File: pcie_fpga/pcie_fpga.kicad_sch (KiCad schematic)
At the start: 18 parts, among them J3 Bus_PCI_Express_x4, U1 XC7A50T-FGG484, U2 LTC6957xMS-2, X1 ECS-2520MVQ-1000-BN-TR

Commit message: brought in the lucanastasio PCIe board template
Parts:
- removed C1, C11, C2, C3, C4, C5, C6, C7, C8, C9: 0.01uf, Capacitor_SMD:C_0603_1608Metric, symbol Device:C
- removed D3: LED, LED_SMD:LED_0603_1608Metric, symbol Device:LED
- removed J3: Bus_PCI_Express_x4, Connector_PCBEdge:BUS_PCIexpress_x4, symbol Connector:Bus_PCI_Express_x4
- removed R2: 49.9, Resistor_SMD:R_0603_1608Metric, symbol Device:R
- removed R3: 240, Resistor_SMD:R_0603_1608Metric, symbol Device:R
- removed U2: LTC6957xMS-2, Package_SO:MSOP-12_3x4mm_P0.65mm, symbol Interface:LTC6957xMS-2
- added J2: PCIexpress_x4, PCIexpress:PCIexpress_x4, symbol PCIexpress:PCIexpress_x4
- R1: value 100 -> 10
- U1: footprint Package_BGA:BGA-484_23.0x23.0mm_Layout22x22_P1.0mm -> Package_BGA:Xilinx_FGG484
- U1: footprint Package_BGA:BGA-484_23.0x23.0mm_Layout22x22_P1.0mm -> (none)
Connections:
- net +3V3: now also J2.A10 (+3.3V), J2.A9 (+3.3V), J2.B8 (+3.3V)
- net GND: now also J2.A12 (GND), J2.A15 (GND), J2.A18 (GND), J2.A20 (GND), J2.A23 (GND), J2.A24 (GND), J2.A27 (GND), J2.A28 (GND), J2.A31 (GND), J2.A4 (GND), J2.B13 (GND), J2.B16 (GND), J2.B18 (GND), J2.B21 (GND), J2.B22 (GND), J2.B25 (GND), J2.B26 (GND), J2.B29 (GND), J2.B32 (GND), J2.B4 (GND), J2.B7 (GND)
- net fpga_clk: now reaches R1.1
- new net +12V: J2.A2 (+12V), J2.A3 (+12V), J2.B1 (+12V), J2.B2 (+12V), J2.B3 (+12V)
- new net +3.3VA: J2.B10 (+3.3V_aux)
- new net prsntn: J2.A1 (~{PRSNT1}), J2.B31 (~{PRSNT2})
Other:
- note added: "From add-in card transmitter to mainboard receiver Place AC coupling capacitors here if necessary"
- note added: "From mainboard transmitter to add-in card receiver Place termination resistors here if necessary"
- note removed: "This is a M-key M.2 connector for an NVMe SSD."
- note removed: "www.hdlguy.com"

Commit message: adding more fpga stuff
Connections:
- net +3V3: now also U1.AA17 (VCCO_13), U1.AB14 (VCCO_13), U1.M14 (VCCO_14), U1.P18 (VCCO_14), U1.R15 (VCCO_14), U1.T22 (VCCO_14), U1.U19 (VCCO_14), U1.V16 (VCCO_13), U1.W13 (VCCO_13), U1.Y10 (VCCO_13), U1.Y20 (VCCO_14)
- net GND: now also U1.A11 (GND), U1.A12 (GND), U1.A2 (GND), U1.A22 (GND), U1.A3 (GND), U1.A5 (GND), U1.A7 (GND), U1.A9 (GND), U1.AA12 (GND), U1.AA2 (GND), U1.AA22 (GND), U1.AB19 (GND), U1.AB9 (GND), U1.B12 (GND), U1.B19 (GND), U1.B3 (GND), U1.C10 (GND), U1.C12 (GND), U1.C16 (GND), U1.C3 (GND), U1.C6 (GND), U1.D12 (GND), U1.D13 (GND), U1.D3 (GND), U1.D4 (GND), U1.D8 (GND), U1.E11 (GND), U1.E12 (VCCBATT_0), U1.E20 (GND), U1.E4 (GND), U1.E5 (GND), U1.E7 (GND), U1.E9 (GND), U1.F11 (GND), U1.F17 (GND), U1.F5 (GND), U1.G10 (GND), U1.G12 (GND), U1.G14 (GND), U1.G5 (GND), U1.G6 (GND), U1.G7 (GND), U1.G8 (GND), U1.G9 (GND), U1.H1 (GND), U1.H11 (GND), U1.H21 (GND), U1.H7 (GND), U1.H9 (GND), U1.J10 (GND), U1.J12 (GND), U1.J18 (GND), U1.J8 (GND), U1.K11 (GND), U1.K15 (GND), U1.K5 (GND), U1.K7 (GND), U1.K9 (GNDADC_0), U1.L2 (GND), U1.L22 (GND), U1.L8 (GND), U1.M11 (GND), U1.M19 (GND), U1.M7 (GND), U1.N16 (GND), U1.N6 (GND), U1.N8 (GND), U1.P11 (GND), U1.P13 (GND), U1.P3 (GND), U1.P7 (GND), U1.P9 (GND), U1.R10 (GND), U1.R12 (GND), U1.R20 (GND), U1.R8 (GND), U1.T11 (GND), U1.T17 (GND), U1.T7 (GND), U1.T9 (GND), U1.U14 (GND), U1.U4 (GND), U1.V1 (GND), U1.V11 (GND), U1.V21 (GND), U1.W18 (GND), U1.W8 (GND), U1.Y15 (GND), U1.Y5 (GND)
- net fpga_clk: now also U1.W19 (IO_L12P_T1_MRCC_14)
- net perstn: now reaches U1.N15 (IO_25_14)
- net perstn: now also J2.A11 (~{PERST})
- net refclk_P: now reaches J2.A13 (REFCLK+)
- net refclk_P: now also U1.F6 (MGTREFCLK0P_216)
- net refclk_N: now reaches J2.A14 (REFCLK-)
- net refclk_N: now also U1.E6 (MGTREFCLK0N_216)
- net per0_P: now reaches J2.A16 (PERp0)
- net per0_P: now also U1.B4 (MGTPTXP0_216)
- net per0_N: now reaches J2.A17 (PERn0)
- net per0_N: now also U1.A4 (MGTPTXN0_216)
- net per1_P: now reaches J2.A21 (PERp1)
- net per1_P: now also U1.D5 (MGTPTXP1_216)
- net per1_N: now reaches J2.A22 (PERn1)
- net per1_N: now also U1.C5 (MGTPTXN1_216)
- net per2_P: now reaches J2.A25 (PERp2)
- net per2_P: now also U1.B6 (MGTPTXP2_216)
- net per2_N: now reaches J2.A26 (PERn2)
- net per2_N: now also U1.A6 (MGTPTXN2_216)
- net per3_P: now reaches J2.A29 (PERp3)
- net per3_P: now also U1.D7 (MGTPTXP3_216)
- net per3_N: now reaches J2.A30 (PERn3)
- net per3_N: now also U1.C7 (MGTPTXN3_216)
- net pet0_P: now reaches J2.B14 (PETp0)
- net pet0_P: now also U1.B8 (MGTPRXP0_216)
- net pet0_N: now reaches J2.B15 (PETn0)
- net pet0_N: now also U1.A8 (MGTPRXN0_216)
- net pet1_P: now reaches J2.B19 (PETp1)
- net pet1_P: now also U1.D11 (MGTPRXP1_216)
- net pet1_N: now reaches J2.B20 (PETn1)
- net pet1_N: now also U1.C11 (MGTPRXN1_216)
- net pet2_P: now reaches J2.B23 (PETp2)
- net pet2_P: now also U1.B10 (MGTPRXP2_216)
- net pet2_N: now reaches J2.B24 (PETn2)
- net pet2_N: now also U1.A10 (MGTPRXN2_216)
- net pet3_P: now reaches J2.B27 (PETp3)
- net pet3_P: now also U1.D9 (MGTPRXP3_216)
- net pet3_N: now reaches J2.B28 (PETn3)
- net pet3_N: now also U1.C9 (MGTPRXN3_216)
- net +1V0: now reaches U1.H10 (VCCINT)
- net +1V0: now also U1.H8 (VCCINT), U1.J11 (VCCBRAM), U1.J7 (VCCINT), U1.J9 (VCCINT), U1.K8 (VCCINT), U1.L11 (VCCBRAM), U1.L7 (VCCINT), U1.M8 (VCCINT), U1.N11 (VCCBRAM), U1.N7 (VCCINT), U1.P10 (VCCINT), U1.P8 (VCCINT), U1.R7 (VCCINT), U1.R9 (VCCINT), U1.T10 (VCCINT), U1.T8 (VCCINT)
- net +1V8: now reaches U1.H12 (VCCAUX)
- net +1V8: now also U1.K10 (VCCADC_0), U1.K12 (VCCAUX), U1.M12 (VCCAUX), U1.P12 (VCCAUX), U1.R11 (VCCAUX)
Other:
- note added: "The PCIe connector is labeled from the perspective of the motherboard. That means the motherboard tx is the fpga rx and vice versa."
- moved on the sheet: J2, R1, U1A, U1B, U1C, U1D, U1E, U1F, U1G, X1

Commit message: looking at Xilinx Artix Ultrascale+ for pcie board
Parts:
- added U2: XCAU10P-1FFVB676I, pedrolib:IC_XCAU10P-1FFVB676I, symbol pedrolib:XCAU10P-1FFVB676I
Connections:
- new net: U2.AA21 (VCCO_64), U2.AB18 (VCCO_64), U2.AD22 (VCCO_64)
- new net: U2.P22 (VCCO_65), U2.U23 (VCCO_65), U2.Y24 (VCCO_65)
- new net: U2.E14 (VCCO_86), U2.H15 (VCCO_86)
- new net: U2.AC15 (VCCO_84), U2.Y14 (VCCO_84)
- new net: U2.A15 (NC_1), U2.A17 (NC_1), U2.A18 (NC_1), U2.A19 (NC_1), U2.A20 (NC_1), U2.A22 (NC_1), U2.A23 (NC_1), U2.A24 (NC_1), U2.A25 (NC_1), U2.A3 (NC_1), U2.A4 (NC_1), U2.B1 (NC_1)
- new net: U2.B15 (NC_2), U2.B16 (NC_2), U2.B17 (NC_2), U2.B19 (NC_2), U2.B2 (NC_2), U2.B20 (NC_2), U2.B21 (NC_2), U2.B22 (NC_2), U2.B24 (NC_2), U2.B6 (NC_2), U2.B7 (NC_2), U2.C3 (NC_2)
- new net: U2.C16 (NC_3), U2.C17 (NC_3), U2.C18 (NC_3), U2.C19 (NC_3), U2.C20 (NC_3), U2.C21 (NC_3), U2.C22 (NC_3), U2.C23 (NC_3), U2.C4 (NC_3), U2.D1 (NC_3), U2.D15 (NC_3), U2.D2 (NC_3), U2.D6 (NC_3), U2.D7 (NC_3)
- new net: U2.D16 (NC_4), U2.D17 (NC_4), U2.D18 (NC_4), U2.D19 (NC_4), U2.D20 (NC_4), U2.D21 (NC_4), U2.E15 (NC_4), U2.E16 (NC_4), U2.E17 (NC_4), U2.E18 (NC_4), U2.E4 (NC_4), U2.E5 (NC_4)
- new net: U2.E20 (NC_5), U2.E21 (NC_5), U2.E22 (NC_5), U2.F15 (NC_5), U2.F17 (NC_5), U2.F18 (NC_5), U2.F19 (NC_5), U2.F20 (NC_5), U2.F6 (NC_5), U2.F7 (NC_5), U2.G15 (NC_5), U2.G16 (NC_5)
- new net: U2.G17 (NC_6), U2.G18 (NC_6), U2.G19 (NC_6), U2.G20 (NC_6), U2.G21 (NC_6), U2.H16 (NC_6), U2.H17 (NC_6), U2.H18 (NC_6), U2.H19 (NC_6), U2.H6 (NC_6), U2.H7 (NC_6), U2.J16 (NC_6), U2.K6 (NC_6), U2.K7 (NC_6)
- new net: U2.A7 (MGTAVTT_R), U2.AB5 (MGTAVTT_R), U2.AE7 (MGTAVTT_R), U2.C7 (MGTAVTT_R), U2.E7 (MGTAVTT_R), U2.F5 (MGTAVTT_R), U2.G7 (MGTAVTT_R), U2.H5 (MGTAVTT_R), U2.K5 (MGTAVTT_R), U2.M5 (MGTAVTT_R), U2.P5 (MGTAVTT_R), U2.T5 (MGTAVTT_R), U2.V5 (MGTAVTT_R), U2.Y5 (MGTAVTT_R)
- new net: U2.AA7 (MGTAVCC_R), U2.AC7 (MGTAVCC_R), U2.J7 (MGTAVCC_R), U2.L7 (MGTAVCC_R), U2.N7 (MGTAVCC_R), U2.W7 (MGTAVCC_R)
- new net: U2.K11 (VCCINT_1), U2.K13 (VCCINT_1), U2.K15 (VCCINT_1), U2.K17 (VCCINT_1), U2.L10 (VCCINT_1), U2.L12 (VCCINT_1), U2.L14 (VCCINT_1), U2.L16 (VCCINT_1), U2.M11 (VCCINT_1), U2.M13 (VCCINT_1)
- new net: U2.L9 (VCCINT_IO), U2.M9 (VCCINT_IO), U2.N9 (VCCINT_IO), U2.P9 (VCCINT_IO)
- new net: U2.M15 (VCCINT_2), U2.M17 (VCCINT_2), U2.N10 (VCCINT_2), U2.N12 (VCCINT_2), U2.N16 (VCCINT_2), U2.P11 (VCCINT_2), U2.P15 (VCCINT_2), U2.P17 (VCCINT_2), U2.R10 (VCCINT_2), U2.R12 (VCCINT_2), U2.R16 (VCCINT_2)
- new net: U2.M18 (VCCAUX), U2.N18 (VCCAUX)
- new net: U2.P18 (VCCAUX_IO), U2.R18 (VCCAUX_IO), U2.T18 (VCCAUX_IO)
- new net: U2.R7 (MGTVCCAUX_R), U2.U7 (MGTVCCAUX_R)
- new net: U2.R9 (VCCBRAM), U2.T9 (VCCBRAM), U2.U9 (VCCBRAM), U2.V9 (VCCBRAM)
- new net: U2.T11 (VCCINT_3), U2.T15 (VCCINT_3), U2.T17 (VCCINT_3), U2.U10 (VCCINT_3), U2.U12 (VCCINT_3), U2.U14 (VCCINT_3), U2.U16 (VCCINT_3), U2.V11 (VCCINT_3), U2.V13 (VCCINT_3), U2.V15 (VCCINT_3), U2.V17 (VCCINT_3)
- new net: U2.E24 (VCCO_66), U2.H25 (VCCO_66), U2.J22 (VCCO_66)
- new net: U2.H20 (GND_9), U2.H8 (GND_9), U2.J1 (GND_9), U2.J17 (GND_9), U2.J2 (GND_9), U2.J3 (GND_9), U2.J6 (GND_9), U2.J8 (GND_9), U2.K12 (GND_9), U2.K3 (GND_9), U2.K4 (GND_9), U2.K8 (GND_9)
- new net: U2.K14 (GND_10), U2.K16 (GND_10), U2.K19 (GND_10), U2.K24 (GND_10), U2.L1 (GND_10), U2.L11 (GND_10), U2.L13 (GND_10), U2.L15 (GND_10), U2.L2 (GND_10), U2.L3 (GND_10), U2.L6 (GND_10), U2.L8 (GND_10)
- new net: U2.L17 (GND_11), U2.L21 (GND_11), U2.L26 (GND_11), U2.M10 (GND_11), U2.M12 (GND_11), U2.M14 (GND_11), U2.M16 (GND_11), U2.M23 (GND_11), U2.M3 (GND_11), U2.M4 (GND_11), U2.M8 (GND_11), U2.N1 (GND_11)
- new net: U2.N11 (GND_12), U2.N15 (GND_12), U2.N17 (GND_12), U2.N2 (GND_12), U2.N20 (GND_12), U2.N25 (GND_12), U2.N3 (GND_12), U2.N6 (GND_12), U2.N8 (GND_12), U2.P10 (GND_12), U2.P3 (GND_12), U2.P4 (GND_12), U2.P8 (GND_12)
- new net: U2.P12 (GND_13), U2.P16 (GND_13), U2.R1 (GND_13), U2.R11 (GND_13), U2.R15 (GND_13), U2.R17 (GND_13), U2.R19 (GND_13), U2.R2 (GND_13), U2.R24 (GND_13), U2.R3 (GND_13), U2.R6 (GND_13), U2.R8 (GND_13)
- new net: U2.T10 (GND_14), U2.T12 (GND_14), U2.T16 (GND_14), U2.T21 (GND_14), U2.T26 (GND_14), U2.T3 (GND_14), U2.T4 (GND_14), U2.T8 (GND_14), U2.U1 (GND_14), U2.U2 (GND_14), U2.U3 (GND_14), U2.U6 (GND_14)
- new net: U2.U11 (GND_15), U2.U13 (GND_15), U2.U15 (GND_15), U2.U17 (GND_15), U2.U18 (GND_15), U2.U8 (GND_15), U2.V10 (GND_15), U2.V12 (GND_15), U2.V14 (GND_15), U2.V3 (GND_15), U2.V4 (GND_15), U2.V8 (GND_15)
- new net: U2.V16 (GND_16), U2.V20 (GND_16), U2.V25 (GND_16), U2.W1 (GND_16), U2.W17 (GND_16), U2.W2 (GND_16), U2.W22 (GND_16), U2.W3 (GND_16), U2.W6 (GND_16), U2.W8 (GND_16), U2.Y19 (GND_16), U2.Y3 (GND_16), U2.Y4 (GND_16), U2.Y8 (GND_16)
- new net: U2.A1 (GND_1), U2.A11 (GND_1), U2.A16 (GND_1), U2.A2 (GND_1), U2.A21 (GND_1), U2.A26 (GND_1), U2.A5 (GND_1), U2.A6 (GND_1), U2.A8 (GND_1), U2.AA1 (GND_1), U2.AA2 (GND_1), U2.AA3 (GND_1)
- new net: U2.AA16 (GND_2), U2.AA26 (GND_2), U2.AA6 (GND_2), U2.AA8 (GND_2), U2.AB13 (GND_2), U2.AB23 (GND_2), U2.AB3 (GND_2), U2.AB4 (GND_2), U2.AB8 (GND_2), U2.AC1 (GND_2), U2.AC2 (GND_2), U2.AC3 (GND_2)
- new net: U2.AC10 (GND_3), U2.AC20 (GND_3), U2.AC25 (GND_3), U2.AC6 (GND_3), U2.AC8 (GND_3), U2.AC9 (GND_3), U2.AD10 (GND_3), U2.AD17 (GND_3), U2.AD3 (GND_3), U2.AD4 (GND_3), U2.AD5 (GND_3), U2.AE1 (GND_3)
- new net: U2.AE10 (GND_4), U2.AE14 (GND_4), U2.AE19 (GND_4), U2.AE2 (GND_4), U2.AE24 (GND_4), U2.AE5 (GND_4), U2.AE6 (GND_4), U2.AF3 (GND_4), U2.AF4 (GND_4), U2.AF5 (GND_4), U2.AF8 (GND_4), U2.AF9 (GND_4)
- new net: U2.AF10 (GND_5), U2.AF11 (GND_5), U2.AF16 (GND_5), U2.AF21 (GND_5), U2.AF26 (GND_5), U2.B13 (GND_5), U2.B18 (GND_5), U2.B23 (GND_5), U2.B3 (GND_5), U2.B4 (GND_5), U2.B5 (GND_5), U2.B8 (GND_5)
- new net: U2.C1 (GND_6), U2.C10 (GND_6), U2.C15 (GND_6), U2.C2 (GND_6), U2.C25 (GND_6), U2.C5 (GND_6), U2.C6 (GND_6), U2.C8 (GND_6), U2.D3 (GND_6), U2.D4 (GND_6), U2.D5 (GND_6), U2.D8 (GND_6)
- new net: U2.D12 (GND_7), U2.D22 (GND_7), U2.E1 (GND_7), U2.E19 (GND_7), U2.E2 (GND_7), U2.E3 (GND_7), U2.E6 (GND_7), U2.E8 (GND_7), U2.F11 (GND_7), U2.F3 (GND_7), U2.F4 (GND_7), U2.F8 (GND_7)
- new net: U2.F16 (GND_8), U2.F21 (GND_8), U2.F26 (GND_8), U2.G1 (GND_8), U2.G13 (GND_8), U2.G2 (GND_8), U2.G23 (GND_8), U2.G3 (GND_8), U2.G6 (GND_8), U2.G8 (GND_8), U2.H3 (GND_8), U2.H4 (GND_8)
- new net: U2.E9 (VCCO_85), U2.H10 (VCCO_85)
- new net: U2.AA11 (VCCO_0), U2.AD12 (VCCO_0)

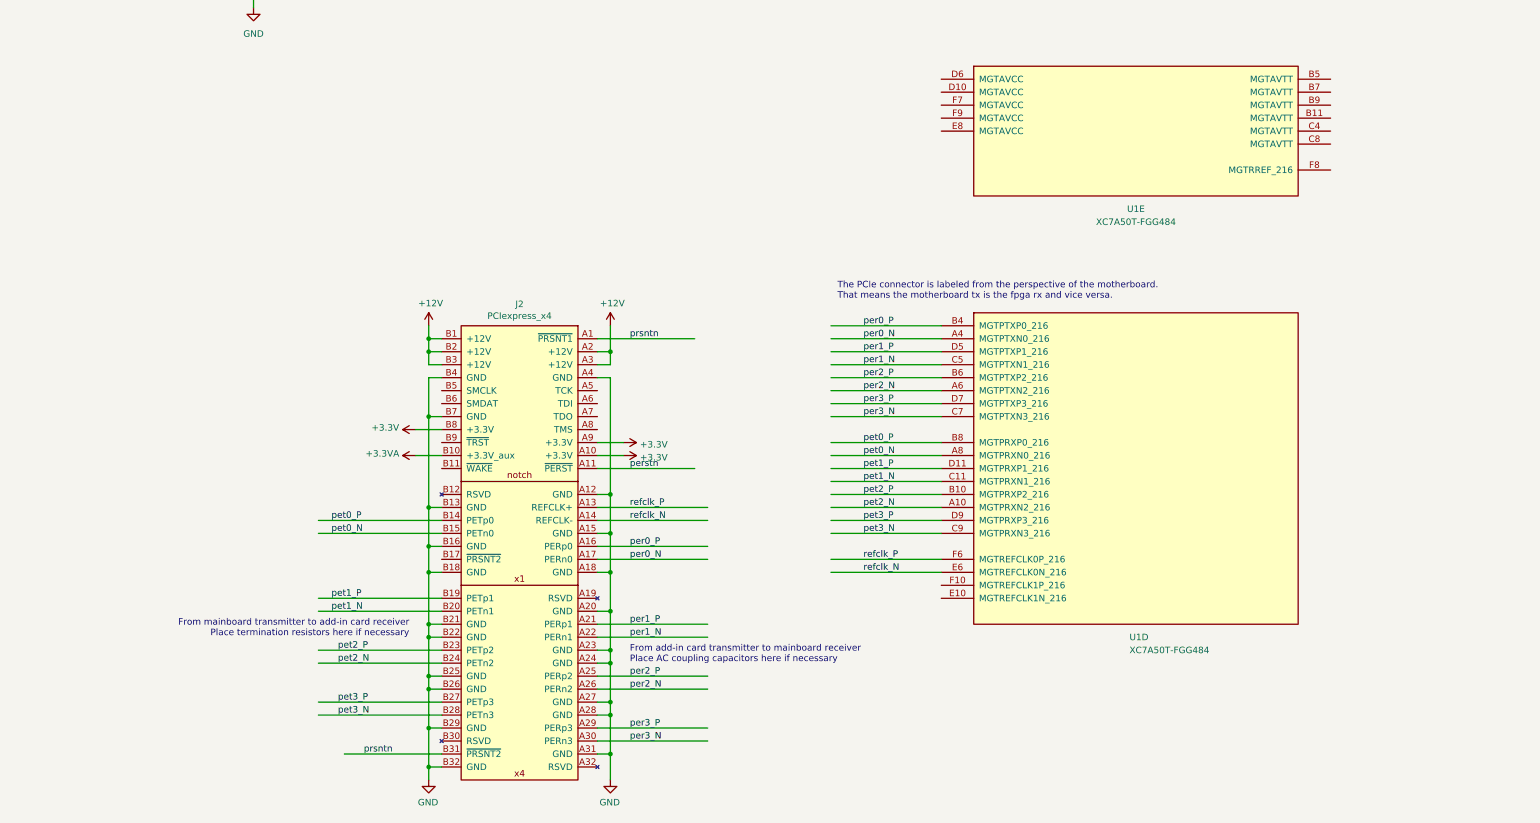
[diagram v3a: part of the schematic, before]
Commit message: x8 PCIe connector
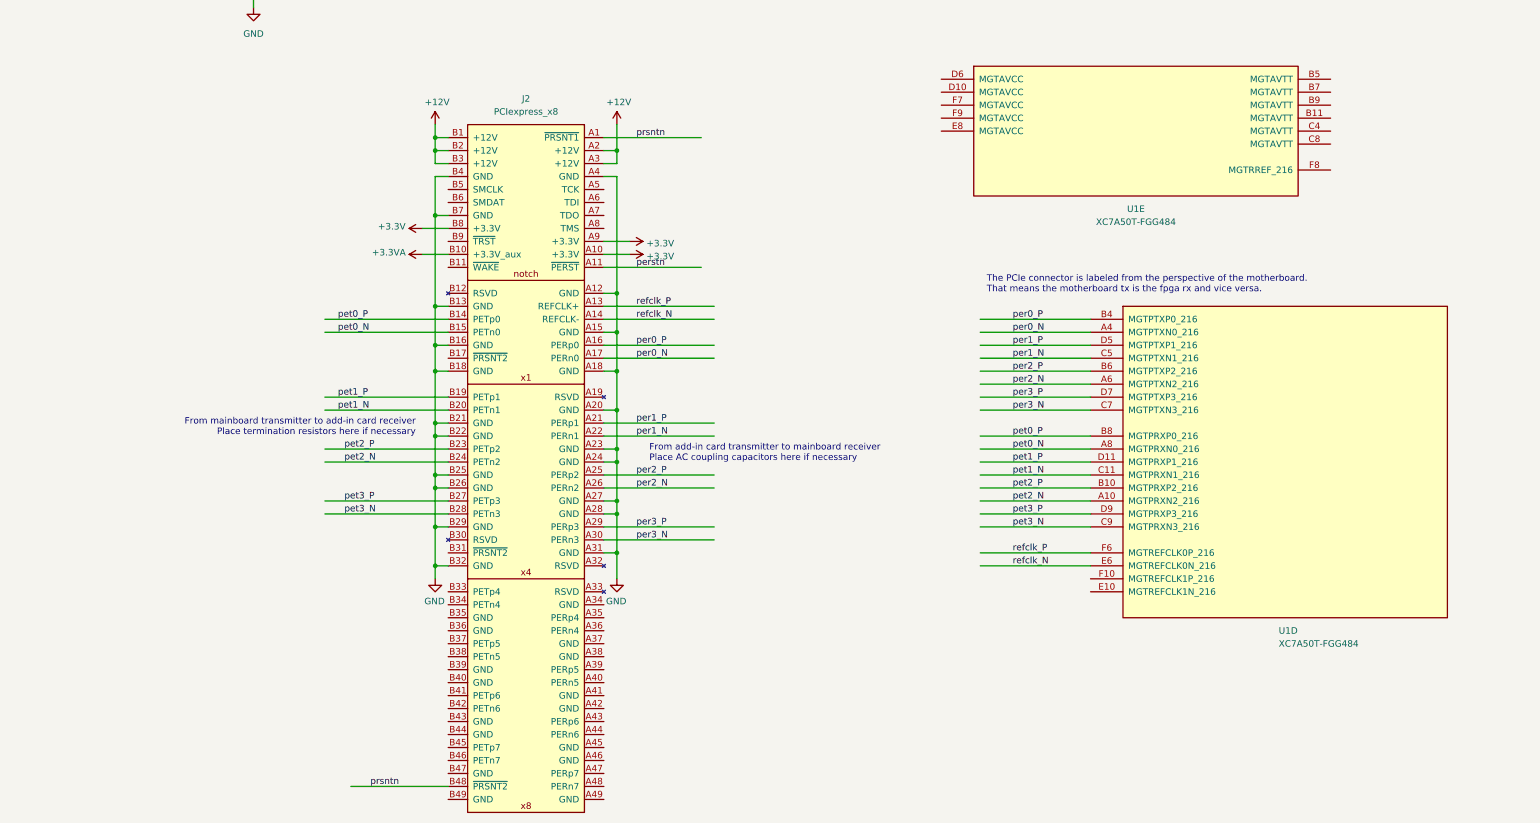
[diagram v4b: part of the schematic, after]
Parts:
- removed J2: PCIexpress_x4, PCIexpress:PCIexpress_x4, symbol PCIexpress:PCIexpress_x4
- added J2: PCIexpress_x8, pedrolib:PCIexpress_x8, symbol pedrolib:PCIexpress_x8
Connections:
- net +12V: now also J2.A2 (+12V), J2.A3 (+12V), J2.B1 (+12V), J2.B2 (+12V), J2.B3 (+12V)
- net +3.3VA: now also J2.B10 (+3.3V_aux)
- net +3V3: now also J2.A10 (+3.3V), J2.A9 (+3.3V), J2.B8 (+3.3V)
- net GND: now also J2.A12 (GND), J2.A15 (GND), J2.A18 (GND), J2.A20 (GND), J2.A23 (GND), J2.A24 (GND), J2.A27 (GND), J2.A28 (GND), J2.A31 (GND), J2.A4 (GND), J2.B13 (GND), J2.B16 (GND), J2.B18 (GND), J2.B21 (GND), J2.B22 (GND), J2.B25 (GND), J2.B26 (GND), J2.B29 (GND), J2.B32 (GND), J2.B4 (GND), J2.B7 (GND)
- net per0_N: now also J2.A17 (PERn0)
- net per0_P: now also J2.A16 (PERp0)
- net per1_N: now also J2.A22 (PERn1)
- net per1_P: now also J2.A21 (PERp1)
- net per2_N: now also J2.A26 (PERn2)
- net per2_P: now also J2.A25 (PERp2)
- net per3_N: now also J2.A30 (PERn3)
- net per3_P: now also J2.A29 (PERp3)
- net perstn: now also J2.A11 (~{PERST})
- net pet0_N: now also J2.B15 (PETn0)
- net pet0_P: now also J2.B14 (PETp0)
- net pet1_N: now also J2.B20 (PETn1)
- net pet1_P: now also J2.B19 (PETp1)
- net pet2_N: now also J2.B24 (PETn2)
- net pet2_P: now also J2.B23 (PETp2)
- net pet3_N: now also J2.B28 (PETn3)
- net pet3_P: now also J2.B27 (PETp3)
- net prsntn: now also J2.A1 (~{PRSNT1}), J2.B48 (~{PRSNT2})
- net refclk_N: now also J2.A14 (REFCLK-)
- net refclk_P: now also J2.A13 (REFCLK+)
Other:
- moved on the sheet: U1D

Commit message: changed out Artix-7 for Artix-UP
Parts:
- removed U1: XC7A50T-FGG484, Package_BGA:Xilinx_FGG484, symbol FPGA_Xilinx_Artix7:XC7A50T-FGG484
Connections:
- net GND: now also J2.A34 (GND), J2.A37 (GND), J2.A38 (GND), J2.A41 (GND), J2.A42 (GND), J2.A45 (GND), J2.A46 (GND), J2.A49 (GND), J2.B35 (GND), J2.B36 (GND), J2.B39 (GND), J2.B40 (GND), J2.B43 (GND), J2.B44 (GND), J2.B47 (GND), J2.B49 (GND), U2.A1 (GND_1), U2.A11 (GND_1), U2.A16 (GND_1), U2.A2 (GND_1), U2.A21 (GND_1), U2.A26 (GND_1), U2.A5 (GND_1), U2.A6 (GND_1), U2.A8 (GND_1), U2.AA1 (GND_1), U2.AA16 (GND_2), U2.AA2 (GND_1), U2.AA26 (GND_2), U2.AA3 (GND_1), U2.AA6 (GND_2), U2.AA8 (GND_2), U2.AB13 (GND_2), U2.AB23 (GND_2), U2.AB3 (GND_2), U2.AB4 (GND_2), U2.AB8 (GND_2), U2.AC1 (GND_2), U2.AC10 (GND_3), U2.AC2 (GND_2), U2.AC20 (GND_3), U2.AC25 (GND_3), U2.AC3 (GND_2), U2.AC6 (GND_3), U2.AC8 (GND_3), U2.AC9 (GND_3), U2.AD10 (GND_3), U2.AD17 (GND_3), U2.AD3 (GND_3), U2.AD4 (GND_3), U2.AD5 (GND_3), U2.AE1 (GND_3), U2.AE10 (GND_4), U2.AE14 (GND_4), U2.AE19 (GND_4), U2.AE2 (GND_4), U2.AE24 (GND_4), U2.AE5 (GND_4), U2.AE6 (GND_4), U2.AF10 (GND_5), U2.AF11 (GND_5), U2.AF16 (GND_5), U2.AF21 (GND_5), U2.AF26 (GND_5), U2.AF3 (GND_4), U2.AF4 (GND_4), U2.AF5 (GND_4), U2.AF8 (GND_4), U2.AF9 (GND_4), U2.B13 (GND_5), U2.B18 (GND_5), U2.B23 (GND_5), U2.B3 (GND_5), U2.B4 (GND_5), U2.B5 (GND_5), U2.B8 (GND_5), U2.C1 (GND_6), U2.C10 (GND_6), U2.C15 (GND_6), U2.C2 (GND_6), U2.C25 (GND_6), U2.C5 (GND_6), U2.C6 (GND_6), U2.C8 (GND_6), U2.D12 (GND_7), U2.D22 (GND_7), U2.D3 (GND_6), U2.D4 (GND_6), U2.D5 (GND_6), U2.D8 (GND_6), U2.E1 (GND_7), U2.E19 (GND_7), U2.E2 (GND_7), U2.E3 (GND_7), U2.E6 (GND_7), U2.E8 (GND_7), U2.F11 (GND_7), U2.F16 (GND_8), U2.F21 (GND_8), U2.F26 (GND_8), U2.F3 (GND_7), U2.F4 (GND_7), U2.F8 (GND_7), U2.G1 (GND_8), U2.G13 (GND_8), U2.G2 (GND_8), U2.G23 (GND_8), U2.G3 (GND_8), U2.G6 (GND_8), U2.G8 (GND_8), U2.H20 (GND_9), U2.H3 (GND_8), U2.H4 (GND_8), U2.H8 (GND_9), U2.J1 (GND_9), U2.J17 (GND_9), U2.J2 (GND_9), U2.J3 (GND_9), U2.J6 (GND_9), U2.J8 (GND_9), U2.K12 (GND_9), U2.K14 (GND_10), U2.K16 (GND_10), U2.K19 (GND_10), U2.K24 (GND_10), U2.K3 (GND_9), U2.K4 (GND_9), U2.K8 (GND_9), U2.L1 (GND_10), U2.L11 (GND_10), U2.L13 (GND_10), U2.L15 (GND_10), U2.L17 (GND_11), U2.L2 (GND_10), U2.L21 (GND_11), U2.L26 (GND_11), U2.L3 (GND_10), U2.L6 (GND_10), U2.L8 (GND_10), U2.M10 (GND_11), U2.M12 (GND_11), U2.M14 (GND_11), U2.M16 (GND_11), U2.M23 (GND_11), U2.M3 (GND_11), U2.M4 (GND_11), U2.M8 (GND_11), U2.N1 (GND_11), U2.N11 (GND_12), U2.N15 (GND_12), U2.N17 (GND_12), U2.N2 (GND_12), U2.N20 (GND_12), U2.N25 (GND_12), U2.N3 (GND_12), U2.N6 (GND_12), U2.N8 (GND_12), U2.P10 (GND_12), U2.P12 (GND_13), U2.P16 (GND_13), U2.P3 (GND_12), U2.P4 (GND_12), U2.P8 (GND_12), U2.R1 (GND_13), U2.R11 (GND_13), U2.R15 (GND_13), U2.R17 (GND_13), U2.R19 (GND_13), U2.R2 (GND_13), U2.R24 (GND_13), U2.R3 (GND_13), U2.R6 (GND_13), U2.R8 (GND_13), U2.T10 (GND_14), U2.T12 (GND_14), U2.T16 (GND_14), U2.T21 (GND_14), U2.T26 (GND_14), U2.T3 (GND_14), U2.T4 (GND_14), U2.T8 (GND_14), U2.U1 (GND_14), U2.U11 (GND_15), U2.U13 (GND_15), U2.U15 (GND_15), U2.U17 (GND_15), U2.U18 (GND_15), U2.U2 (GND_14), U2.U3 (GND_14), U2.U6 (GND_14), U2.U8 (GND_15), U2.V10 (GND_15), U2.V12 (GND_15), U2.V14 (GND_15), U2.V16 (GND_16), U2.V20 (GND_16), U2.V25 (GND_16), U2.V3 (GND_15), U2.V4 (GND_15), U2.V8 (GND_15), U2.W1 (GND_16), U2.W17 (GND_16), U2.W2 (GND_16), U2.W22 (GND_16), U2.W3 (GND_16), U2.W6 (GND_16), U2.W8 (GND_16), U2.Y19 (GND_16), U2.Y3 (GND_16), U2.Y4 (GND_16), U2.Y8 (GND_16)
- net per4_P: now reaches J2.A35 (PERp4)
- net per4_N: now reaches J2.A36 (PERn4)
- net per5_P: now reaches J2.A39 (PERp5)
- net per5_N: now reaches J2.A40 (PERn5)
- net per6_P: now reaches J2.A43 (PERp6)
- net per6_N: now reaches J2.A44 (PERn6)
- net per7_P: now reaches J2.A47 (PERp7)
- net per7_N: now reaches J2.A48 (PERn7)
- net pet4_P: now reaches J2.B33 (PETp4)
- net pet4_N: now reaches J2.B34 (PETn4)
- net pet5_P: now reaches J2.B37 (PETp5)
- net pet5_N: now reaches J2.B38 (PETn5)
- net pet6_P: now reaches J2.B41 (PETp6)
- net pet6_N: now reaches J2.B42 (PETn6)
- net pet7_P: now reaches J2.B45 (PETp7)
- net pet7_N: now reaches J2.B46 (PETn7)
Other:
- note added: "From mainboard transmitter to add-in card receiver."
- note removed: "From mainboard transmitter to add-in card receiver Place termination resistors here if necessary"
- moved on the sheet: U2A, U2B, U2C, U2D, U2E, U2F, U2G, U2H, U2I, U2J, U2K, U2L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
